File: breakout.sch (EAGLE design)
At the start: 11 parts, among them IC2 REG1117

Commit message: Tidy up for publishing
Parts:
- added FRAME1: (no value), SparkFun-Aesthetics:FRAME-LETTERNO_PACKAGE
- added LOGO1: OSHW-LOGOS, SparkFun-Aesthetics:OSHW-LOGOS
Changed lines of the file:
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@@
 <layer number="112" name="tSilk" color="7" fill="1" visible="yes" active="yes"/>
 <layer number="113" name="IDFDebug" color="4" fill="1" visible="yes" active="yes"/>
+<layer number="114" name="FRNTMAAT1" color="7" fill="1" visible="yes" active="yes"/>
+<layer number="115" name="FRNTMAAT2" color="7" fill="1" visible="yes" active="yes"/>
 <layer number="116" name="Patch_BOT" color="9" fill="4" visible="no" active="yes"/>
+<layer number="117" name="BACKMAAT1" color="7" fill="1" visible="yes" active="yes"/>
+<layer number="118" name="Rect_Pads" color="7" fill="1" visible="no" active="no"/>
+<layer number="119" name="KAP_TEKEN" color="7" fill="1" visible="yes" active="yes"/>
+<layer number="120" name="KAP_MAAT1" color="7" fill="1" visible="yes" active="yes"/>
 <layer number="121" name="_tsilk" color="7" fill="1" visible="no" active="yes"/>
 <layer number="122" name="_bsilk" color="7" fill="1" visible="no" active="yes"/>
@@
 <layer number="128" name="_bValues" color="7" fill="1" visible="yes" active="yes"/>
 <layer number="129" name="Mask" color="7" fill="1" visible="yes" active="yes"/>
+<layer number="130" name="SMDSTROOK" color="7" fill="1" visible="yes" active="yes"/>
 <layer number="131" name="tAdjust" color="7" fill="1" visible="yes" active="yes"/>
 <layer number="132" name="bAdjust" color="7" fill="1" visible="yes" active="yes"/>
@@
 <layer number="230" name="230bmp" color="7" fill="1" visible="yes" active="yes"/>
 <layer number="231" name="231bmp" color="7" fill="1" visible="yes" active="yes"/>
+<layer number="232" name="Eagle3D_PG2" color="7" fill="1" visible="no" active="no"/>
+<layer number="233" name="Eagle3D_PG3" color="7" fill="1" visible="no" active="no"/>
 <layer number="248" name="Housing" color="7" fill="1" visible="yes" active="yes"/>
 <layer number="249" name="Edge" color="7" fill="1" visible="yes" active="yes"/>
@@
 <part name="C1" library="SparkFun-Capacitors" deviceset="CAP" device="1206" value="0.1uf"/>
 <part name="C2" library="SparkFun-Capacitors" deviceset="CAP" device="1206" value="0.1uf"/>
-<part name="GND1" library="supply1" deviceset="GND" device=""/>
 <part name="GND2" library="supply1" deviceset="GND" device=""/>
 <part name="GND3" library="supply1" deviceset="GND" device=""/>
@@
 <part name="GND7" library="supply1" deviceset="GND" device=""/>
 <part name="GND8" library="supply1" deviceset="GND" device=""/>
-<part name="GND9" library="supply1" deviceset="GND" device=""/>
 <part name="IC2" library="burr-brown" deviceset="REG1117" device=""/>
 <part name="SUPPLY1" library="SparkFun-Aesthetics" deviceset="3.3V" device=""/>
-<part name="SUPPLY2" library="SparkFun-Aesthetics" deviceset="3.3V" device=""/>
 <part name="SUPPLY3" library="SparkFun-Aesthetics" deviceset="3.3V" device=""/>
 <part name="SUPPLY4" library="SparkFun-Aesthetics" deviceset="3.3V" device=""/>
 <part name="SUPPLY5" library="SparkFun-Aesthetics" deviceset="3.3V" device=""/>
 <part name="SUPPLY6" library="SparkFun-Aesthetics" deviceset="3.3V" device=""/>
-<part name="SUPPLY7" library="SparkFun-Aesthetics" deviceset="3.3V" device=""/>
 <part name="SUPPLY8" library="SparkFun-Aesthetics" deviceset="3.3V" device=""/>
-<part name="SUPPLY9" library="SparkFun-Aesthetics" deviceset="5V" device=""/>
-<part name="SUPPLY10" library="SparkFun-Aesthetics" deviceset="5V" device=""/>
-<part name="SUPPLY11" library="SparkFun-Aesthetics" deviceset="5V" device=""/>
 <part name="SUPPLY12" library="SparkFun-Aesthetics" deviceset="5V" device=""/>
 <part name="SUPPLY13" library="SparkFun-Aesthetics" deviceset="5V" device=""/>
@@
 <part name="R4" library="SparkFun-Resistors" deviceset="RESISTOR" device="1206" value="10k"/>
 <part name="R5" library="SparkFun-Resistors" deviceset="RESISTOR" device="1206" value="10k"/>
+<part name="LOGO1" library="SparkFun-Aesthetics" deviceset="OSHW-LOGO" device="S"/>
+<part name="FRAME1" library="SparkFun-Aesthetics" deviceset="FRAME-LETTER" device="NO_PACKAGE"/>
 </parts>
 <sheets>
@@
 <instance part="C1" gate="G$1" x="66.04" y="83.82"/>
 <instance part="C2" gate="G$1" x="78.74" y="83.82"/>
-<instance part="GND1" gate="1" x="-10.16" y="88.9"/>
 <instance part="GND2" gate="1" x="53.34" y="76.2"/>
 <instance part="GND3" gate="1" x="43.18" y="20.32"/>
@@
 <instance part="GND7" gate="1" x="121.92" y="73.66"/>
 <instance part="GND8" gate="1" x="-2.54" y="63.5"/>
-<instance part="GND9" gate="1" x="-7.62" y="88.9"/>
 <instance part="IC2" gate="G$1" x="121.92" y="91.44"/>
 <instance part="SUPPLY1" gate="G$1" x="53.34" y="104.14"/>
-<instance part="SUPPLY2" gate="G$1" x="-7.62" y="96.52"/>
 <instance part="SUPPLY3" gate="G$1" x="137.16" y="93.98"/>
 <instance part="SUPPLY4" gate="G$1" x="-12.7" y="58.42"/>
 <instance part="SUPPLY5" gate="G$1" x="66.04" y="91.44"/>
 <instance part="SUPPLY6" gate="G$1" x="48.26" y="55.88"/>
-<instance part="SUPPLY7" gate="G$1" x="-10.16" y="96.52"/>
 <instance part="SUPPLY8" gate="G$1" x="-2.54" y="93.98"/>
-<instance part="SUPPLY9" gate="G$1" x="-12.7" y="104.14"/>
-<instance part="SUPPLY10" gate="G$1" x="-10.16" y="104.14"/>
-<instance part="SUPPLY11" gate="G$1" x="-7.62" y="104.14"/>
 <instance part="SUPPLY12" gate="G$1" x="-17.78" y="58.42"/>
 <instance part="SUPPLY13" gate="G$1" x="78.74" y="91.44"/>
@@
 <instance part="R4" gate="G$1" x="17.78" y="76.2"/>
 <instance part="R5" gate="G$1" x="17.78" y="68.58"/>
+<instance part="LOGO1" gate="G$1" x="-30.48" y="-27.94"/>
+<instance part="FRAME1" gate="G$1" x="-45.72" y="-40.64"/>
 </instances>
 <busses>

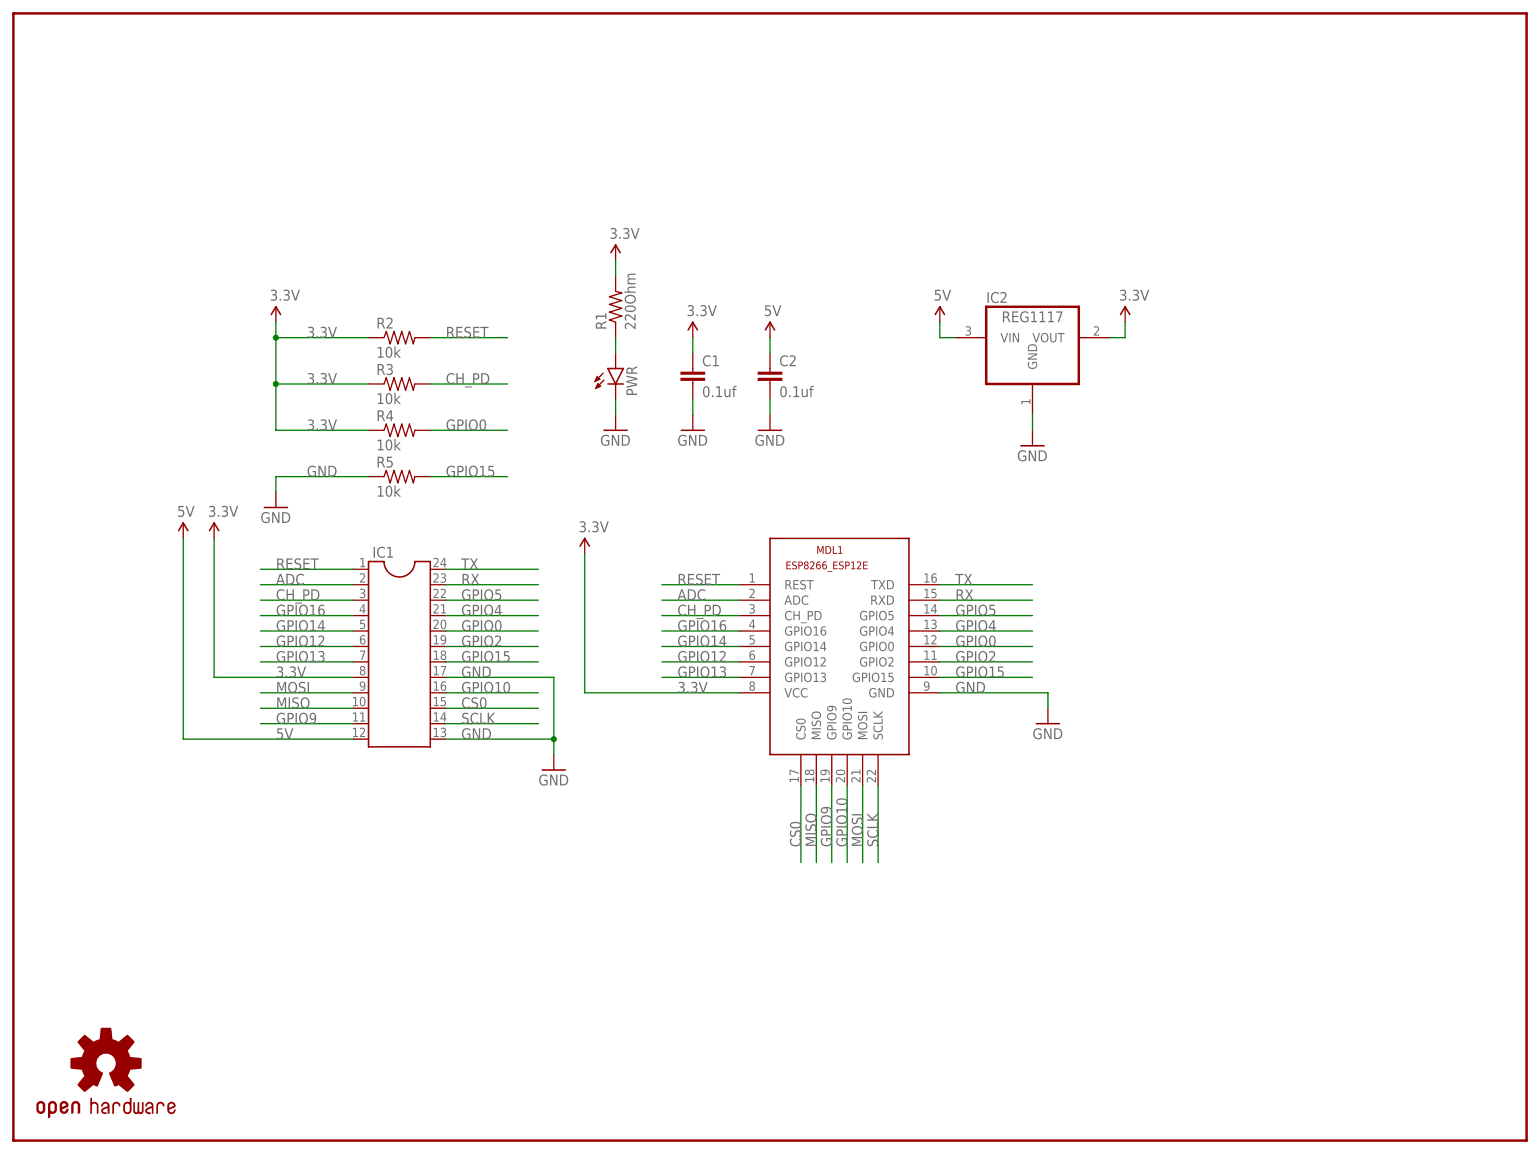
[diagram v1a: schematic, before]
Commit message: Added FTDI + USB support on the board. Also cleaned up the schematic. DRC pass.
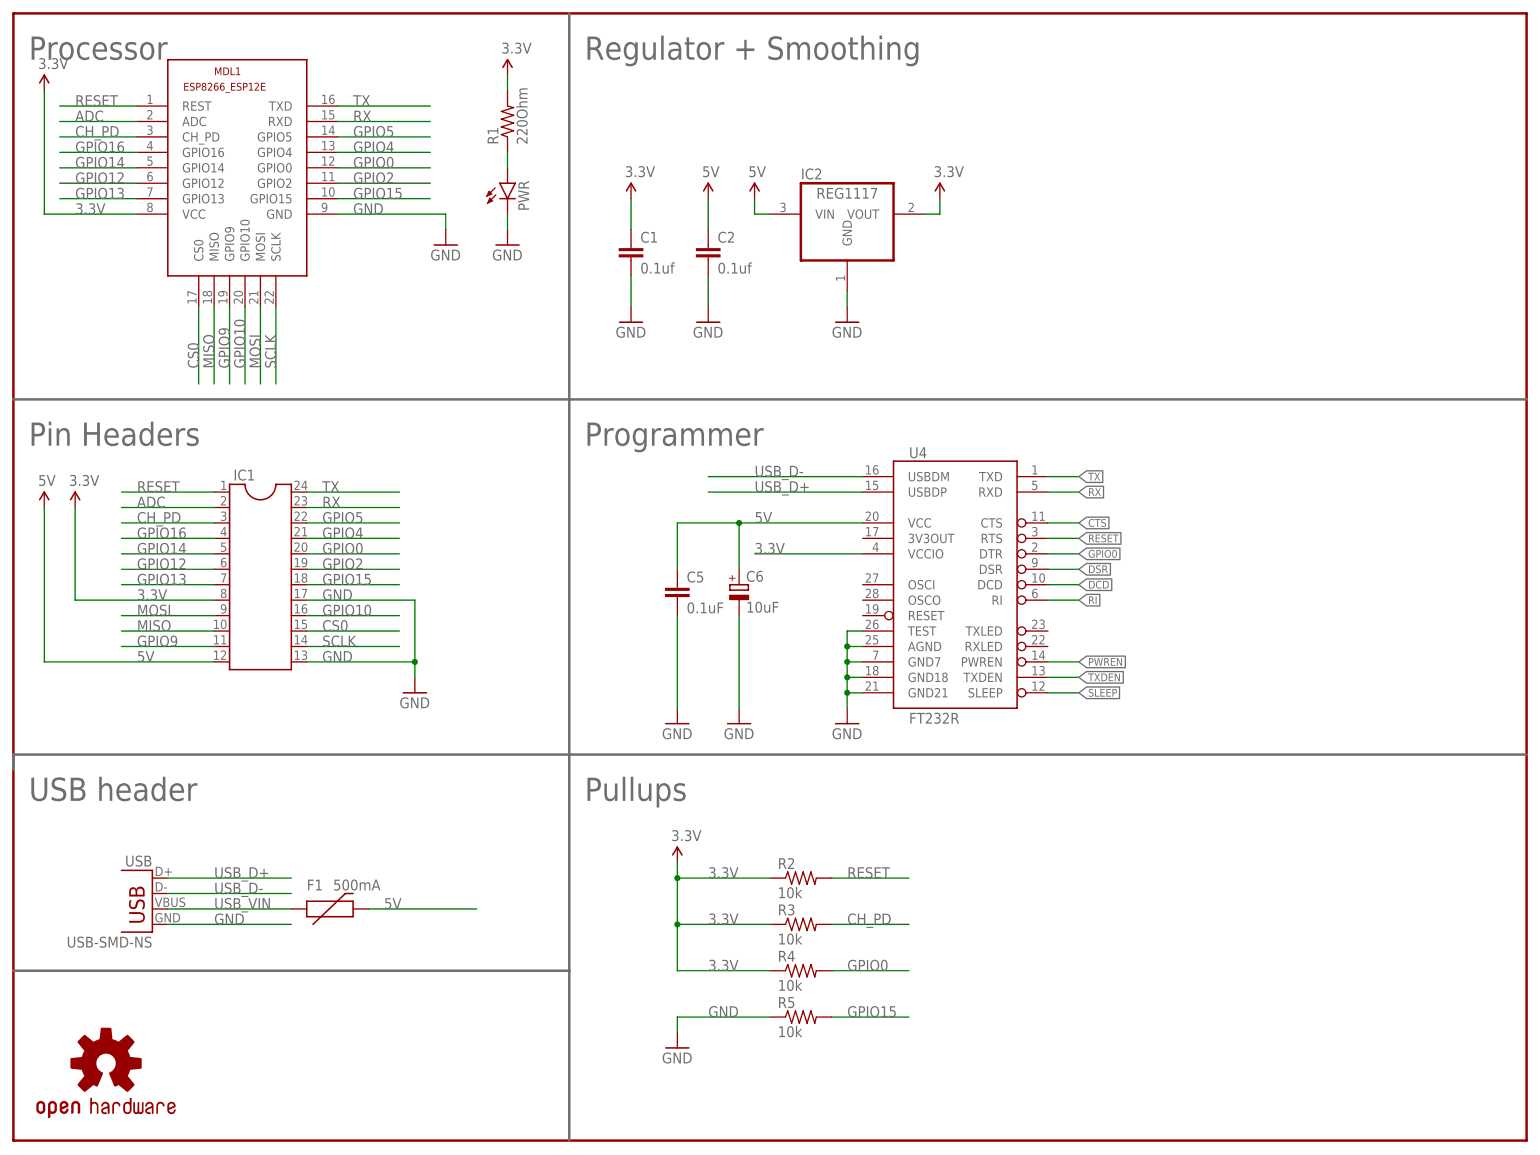
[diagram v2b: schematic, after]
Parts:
- added C5: 0.1uF, rcl:C-EUC1206K
- added C6: 10uF, rcl:CPOL-EUSMCA
- added F1: 500mA, SparkFun:PTCSMD
- added U4: FT232R, SparkFun:FT232RLSSOP
- added USB: USB-SMD-NS, SparkFun-Connectors:USB-SMD-NS
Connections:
- new net CTS: U4.CTS
- new net DCD: U4.DCD
- new net DSR: U4.DSR
- new net PWREN: U4.PWREN
- new net RI: U4.RI
- new net SLEEP: U4.SLEEP
- new net TXDEN: U4.TXDEN
- new net USB_D+: U4.USBDP, USB.D+
- new net USB_D-: U4.USBDM, USB.D-
- new net USB_VIN: F1.1, USB.VBUS
- net 3.3V: now also U4.VCCIO
- net 5V: now also C5.1, C6.+, F1.2, U4.VCC
- net GND: now also C5.2, C6.-, U4.AGND, U4.GND18, U4.GND21, U4.GND7, U4.TEST, USB.GND
- net GPIO0: now also U4.DTR
- net RESET: now also U4.RTS
- net RX: now also U4.RXD
- net TX: now also U4.TXD
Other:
- note added: "Pin Headers"
- note added: "Processor"
- note added: "Programmer"
- note added: "Pullups"
- note added: "Regulator + Smoothing"
- note added: "USB header"
- moved on the sheet: C1, C2, IC1, IC2, MDL1, PWR, R1, R2, R3, R4, R5

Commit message: Revision to switch around TX/RX lines so that this thing actually works, detach RTS signal from RESET, add TX & RX LEDs + assoc. resistors. Renamed GPIO4 & GPIO5 as SDA and SCL respectively to suit their default i2c states.
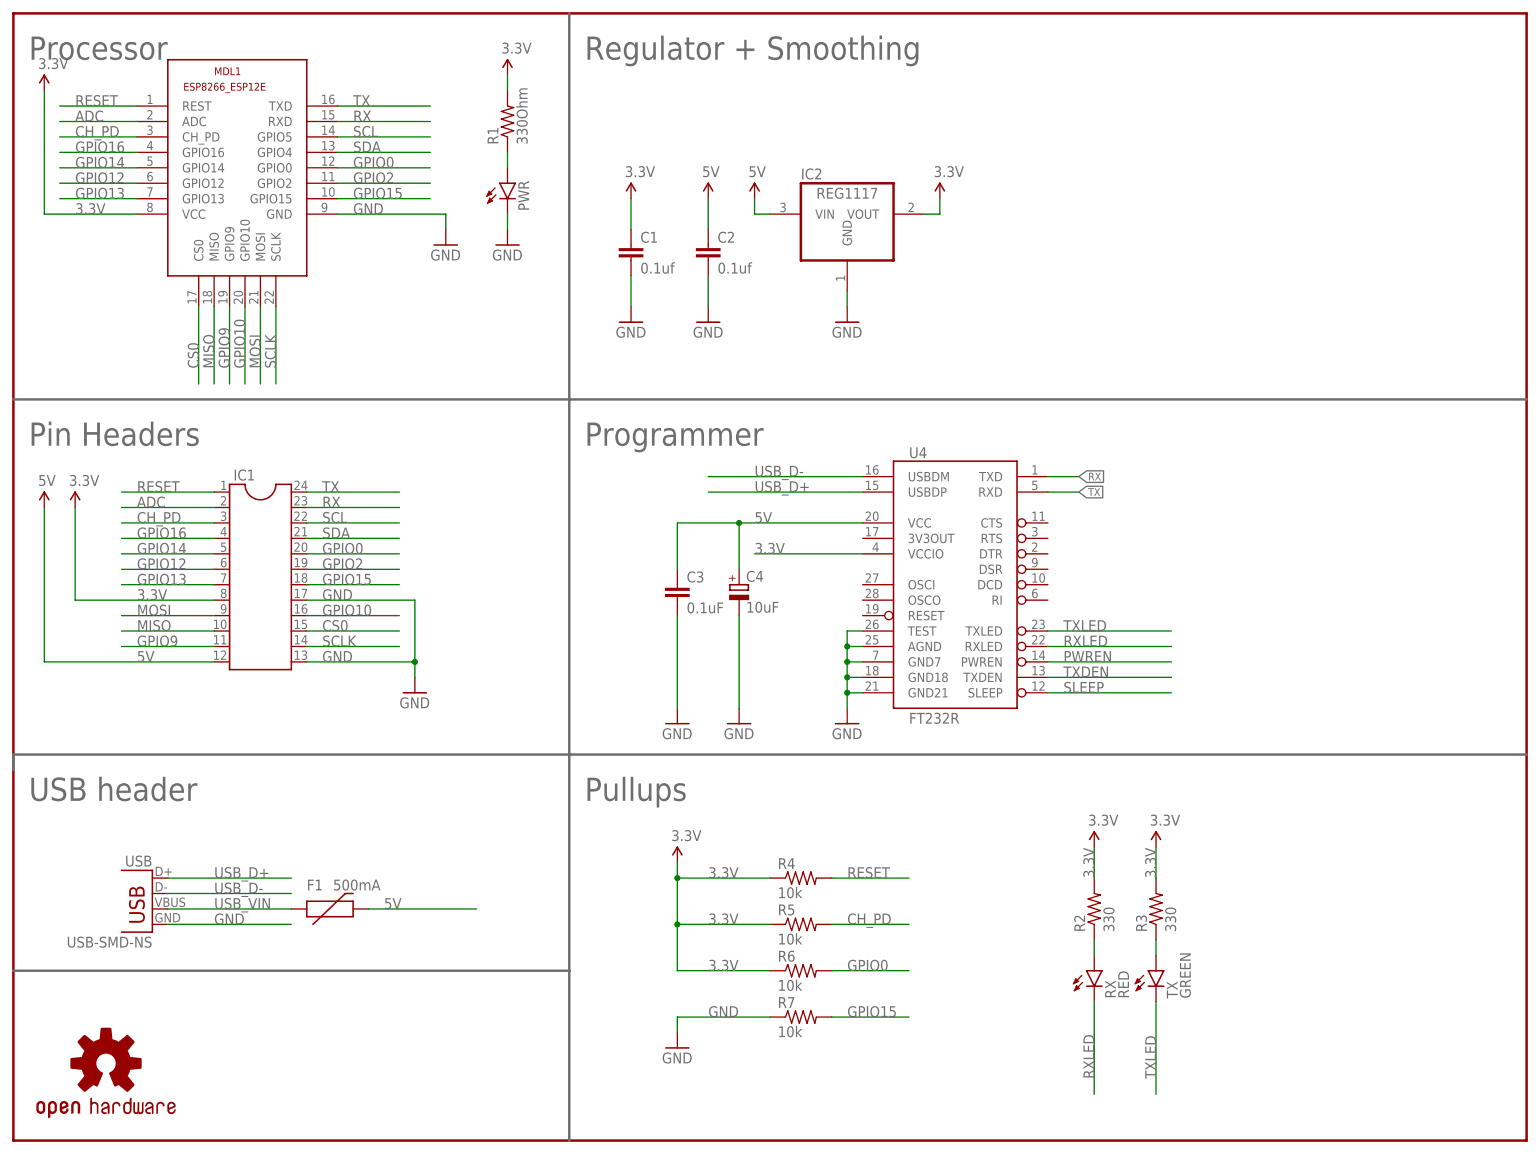
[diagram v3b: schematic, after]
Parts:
- added R6, R7: 10k, SparkFun-Resistors:RESISTOR1206
- added RX: RED, SparkFun-LED:LED1206
- added TX: GREEN, SparkFun-LED:LED1206
- R1: value 220Ohm -> 330Ohm
- R2, R3: value 10k -> 330; device SparkFun-Resistors:RESISTOR1206 -> SparkFun-Passives:RESISTOR1206
- renumbered C5 to C3, C6 to C4
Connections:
- net GPIO4 renamed SDA
- net GPIO5 renamed SCL
- removed net CTS: U4.CTS
- removed net DCD: U4.DCD
- removed net DSR: U4.DSR
- removed net RI: U4.RI
- new net N$2: R2.1, RX.A
- new net N$3: R3.1, TX.A
- new net RXLED: RX.C, U4.RXLED
- new net TXLED: TX.C, U4.TXLED
- net 3.3V: now also R2.2, R3.2, R5.1, R6.1; no longer R2.1, R3.1
- net CH_PD: now also R5.2; no longer R3.2
- net GND: now also R7.1; no longer R5.1
- net GPIO0: now also R6.2; no longer R4.2, U4.DTR
- net GPIO15: now also R7.2; no longer R5.2
- net RESET: now also R4.2; no longer R2.2, U4.RTS
- net RX: now also U4.TXD; no longer U4.RXD
- net TX: now also U4.RXD; no longer U4.TXD
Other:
- moved on the sheet: R2, R3, R4, R5
